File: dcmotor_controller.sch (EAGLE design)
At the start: 69 parts, among them IC1 L298, IC2 L298, IC3 AS5040, IC4 7805DT, IC5 SN74LVCR162245A, Q1 8MHz, U1 STM32F051C8T6

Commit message: Add files via upload
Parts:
- removed C15: 4u7, rcl:C-EU025-024X044
- removed C17, C18: 100n, rcl:C-EU025-024X044
- removed C19: 1u, rcl:C-EU025-024X044
- removed C23, C24: (no value), rcl:C-EU025-024X044
- removed C6: 10uF, rcl:CPOL-EUE1.8-4
- removed C7, C8: 1uF, rcl:CPOL-EUE1.8-4
- removed IC3: AS5040, austriamicrosystems:AS5040
- removed IC4: 7805DT, linear:7805DT
- removed LED1: (no value), led:LED
- removed R1: 10k, rcl:R-EU_0204/2V
- removed R17, R18: 10k, resistor:R-EU_0204/5
- removed R2: 330, rcl:R-EU_0204/2V
- removed R9: 4.7k, rcl:R-EU_0204/2V
- removed SV1: (no value), con-ml:ML10L
- removed U1: STM32F051C8T6, untitled:STM32F051C8T6
- added C25: 4u7, rcl:C-EU025-024X044
- added C26, C27, C28, C30: 100n, rcl:C-EU025-024X044
- added C29: 1u, rcl:C-EU025-024X044
- added C31, C32: 20p, rcl:C-EU025-024X044
- added D19: SK38SMA, diode:DIODE-DO214AC
- added F2: 2920L050, polyfuse-smd_10:2920L050
- added LED, POWER_CON: (no value), con-ptr500:AK500/2
- added LED2: (no value), led:LEDCHIPLED_0805
- added Q2: 8MHz, crystal:CSM-7X-DU
- added R19: 1.2k, 0.5W, rcl:R-EU_R2010
- added R20: 0R25, rcl:R-EU_R2512
- added R45, R63: 10k, resistor:R-EU_M0805
- added R46: 2k2, resistor:R-EU_M0805
- added R48: 100k, resistor:R-EU_M0805
- added R49: 100, resistor:R-EU_M0805
- added SV2, SV3, SV4, SV5: (no value), con-ml:ML10L
- added SV6: (no value), con-lsta:FE20-2
- added T1: BC857BS, NXP_60_26022015:BC857BS
- added T14: BSS306N, we-transistor:MOSFET-N-SOT23
- added U$1: DC-DC-STEP-DOWN-LM2596, lm2596:DC-DC-STEP-DOWN-LM2596
- added U2: STM32F10XRXT6, stm32:STM32F10XRXT6
- added X3: (no value), con-phoenix-254:MPT2
- C1: device capacitor-wima:C2,5-3 -> rcl:C-EUC0805
- C10: value 10u -> 100u; device rcl:CPOL-EU140CLH-0810 -> resistor:CPOL-EU153CLV-0807; LINK (none) -> http://www.tme.eu/pl/details/sc1e107m0806bvr/kondensatory-e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
- C11, C12, C13, C14: device capacitor-wima:C2.5/2 -> resistor:C-EUC0805
- C16: device rcl:C-EU025-024X044 -> resistor:C-EUC0805
- C2: device capacitor-wima:C2.5/4 -> rcl:C-EUC0805
- C20: value 100n -> 47u; device rcl:C-EU025-024X044 -> resistor:C-EUC0805; LINK (none) -> http://www.tme.eu/pl/details/cl21a476mqynnng/kondensatory-m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
- C21, C22: value 20p -> 100n; device rcl:C-EU025-024X044 -> resistor:C-EUC0805
- C3: device capacitor-wima:C2,5-3 -> resistor:C-EUC0805
- C4: device capacitor-wima:C2.5/4 -> resistor:C-EUC0805
- C5: value 100n -> (none); device capacitor-wima:C2,5-3 -> rcl:C-EUC0805
- C9: value 100u -> 4u7; device rcl:CPOL-EU140CLH-0810 -> resistor:C-EUC0805
- D10, D11, D12, D13, D14, D15, D16, D2, D3, D4, D5, D6, D7, D8, D9: value GF1 -> SK38SMA; device diode:GF1 -> diode:DIODE-DO214AC; LINK (none) -> http://www.tme.eu/pl/details/sk38sma-dio/diody-schottky-smd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
- D17: value GF1 -> SMBJ5.0A-TR; device diode:GF1 -> diode:SUPPRESSOR-SMBJ
- Q1: value 8MHz -> MOSFET-PCHANNEL_SOT23-3; device crystal:CSM-7X-DU -> Simplex-DiscreteSemi:MOSFET-PCHANNEL_SOT23-3
- R15, R16: device resistor:R-EU_0204/5 -> resistor:R-EU_M0805
- R3, R4, R5: device rcl:R-EU_0204/5 -> rcl:R-EU_R2512; LINK (none) -> http://www.tme.eu/pl/details/cs2512-0r25-1%25-hp/rezystory-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
- R6: value 0R25 -> 10k; device rcl:R-EU_0204/5 -> resistor:R-EU_M0805
- R7, R8: value 4.7k -> 10k 1%; device rcl:R-EU_0204/2V -> resistor:R-EU_M0805
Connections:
- removed net A_LSB_U: IC3.A_LSB_U, SV1.2
- removed net B_DIR_V: IC3.B_DIR_V, SV1.3
- removed net D0: IC3.D0, SV1.7
- removed net INDEX_W: IC3.INDEX_W, SV1.4
- removed net N$1: IC3.MAGDEC, IC3.MAGINC, R1.1, R2.2
- removed net N$10: C7.+, R8.1, R9.2
- removed net N$13: C6.+, IC3.VDD3V3
- removed net N$2: LED1.A, R2.1
- removed net PROGRAM: IC3.PROG
- removed net PWM: IC3.PWN, R8.2, SV1.9
- removed net PWM_F: C8.+, R9.1, SV1.8
- removed net VCC: C1.2, C10.+, C2.1, C3.2, C4.1, C5.1, D11.C, D13.C, D15.C, D16.C, D3.C, D5.C, D7.C, D9.C, IC1.VCC, IC1.VS, IC2.VCC, IC2.VS, IC3.VDD5V, IC4.VO, R1.2, R10.2, R11.2, R12.2, R14.2, SV1.1
- removed net VDD: C15.1, C16.1, C17.1, C18.1, C19.1, C20.1, U1A.VDD, U1A.VDDA, U1B.VDD
- new net +3V3: SV6.17
- new net 24V: C10.+, C2.1, C4.1, C9.1, D19.C, D2.C, D3.C, D4.C, D5.C, D6.C, D7.C, D8.C, IC1.VS, IC2.VS, LED-2.KL, POWER_CON-2.KL, R19.1, R45.2, U$1.IN+, X3-1.1
- new net A_LSB_U1: SV2.2, U2PORTA_H.PA8
- new net A_LSB_U2: SV3.2, U2PORTA_H.PA9
- new net A_LSB_U3: SV4.2, U2PORTA_H.PA10
- new net A_LSB_U4: SV5.2, U2PORTA_H.PA11
- new net B_DIR_V1: SV2.3, U2PORTC_H.PC8
- new net B_DIR_V2: SV3.3, U2PORTC_H.PC9
- new net B_DIR_V3: SV4.3, U2PORTC_H.PC10
- new net B_DIR_V4: SV5.3, U2PORTC_H.PC11
- new net D01: SV2.7
- new net D02: SV3.7
- new net D03: SV4.7
- new net D04: SV5.7
- new net INDEX_W1: SV2.4, U2PORTB_H.PB12
- new net INDEX_W2: SV3.4, U2PORTB_H.PB13
- new net INDEX_W3: SV4.4, U2PORTB_H.PB14
- new net INDEX_W4: SV5.4, U2PORTB_H.PB15
- new net MISO: U2PORTB_L.PB4
- new net MOSI: U2PORTB_L.PB5
- new net N$16: U2AN_POWER.VBAT
- new net N$19: Q1.G, R8.2, T1-2.C
- new net N$20: R7.2, T1-1.B, T1-1.C, T1-2.B
- new net N$21: R48.2, R49.1, T14.G
- new net N$24: LED-1.KL, T14.D
- new net OSC_IN: C31.2, Q2.2, U2PORTD/OSC.PD0/OSC<=
- new net OSC_OUT: C32.2, Q2.1, U2PORTD/OSC.PD1/OSC=>
- new net PWM1: SV2.9
- new net PWM2: SV3.9
- new net PWM3: SV4.9
- new net PWM4: SV5.9
- new net PWM_F1: SV2.8
- new net PWM_F2: SV3.8
- new net PWM_F3: SV4.8
- new net PWM_F4: SV5.8
- new net SCK: U2PORTB_L.PB3
- net 3V3: now also C22.2, C25.1, C26.1, C27.1, C28.1, C29.1, C30.1, R10.2, R11.2, R12.2, R14.2, SV2.1, SV3.1, SV4.1, SV5.1, SV6.1, U2AN_POWER.VDDA, U2POWER.VDD_1, U2POWER.VDD_2, U2POWER.VDD_3, U2POWER.VDD_4; no longer C24.1
- net 5V: now also C1.2, C14.2, C16.1, C3.2, D17.C, IC1.VCC, IC2.VCC, Q1.S, SV6.2, SV6.4, T1-2.E; no longer C23.1
- net BAT_MEAS: now also C20.1, R45.1, R46.2, U2PORTA_L.PA4; no longer U1A.PA4
- net BOOTO: now also U2RESET.BOOT0; no longer U1B.BOOT0
- net CLK: now also SV2.6, SV3.6, SV4.6, SV5.6; no longer IC3.CLK, SV1.6
- net CSN: now also SV2.5, SV3.5, SV4.5, SV5.5; no longer IC3.CSN, R7.2, SV1.5
- net EN1_UC: now also U2PORTA_L.PA6; no longer U1A.PA6
- net EN2_UC: now also U2PORTA_L.PA7; no longer U1A.PA7
- net EN3_UC: now also U2PORTB_L.PB0; no longer U1A.PB0
- net EN4_UC: now also U2PORTB_L.PB1; no longer U1A.PB1
- net GND: now also C11.1, C12.1, C13.1, C14.1, C25.2, C26.2, C27.2, C28.2, C29.2, C30.2, C31.1, C32.1, C9.2, D11.A, D13.A, D15.A, D16.A, D9.A, LED2.C, POWER_CON-1.KL, R20.1, R46.1, R48.1, R63.2, R8.1, SV2.10, SV3.10, SV4.10, SV5.10, SV6.14, SV6.20, SV6.25, SV6.30, SV6.34, SV6.39, SV6.6, SV6.9, T14.S, U$1.IN-, U$1.OUT-, U2AN_POWER.VSSA, U2POWER.VSS_1, U2POWER.VSS_2, U2POWER.VSS_3, U2POWER.VSS_4, X3-2.1; no longer C11.2, C12.2, C13.2, C14.2, C15.2, C17.2, C18.2, C19.2, C23.2, C24.2, C6.-, C7.-, C8.-, C9.-, D2.A, D4.A, D6.A, D8.A, IC3.VSS, IC4.GND, LED1.C, R17.2, R18.1, SV1.10, U1A.VSS, U1A.VSSA, U1B.VSS
- net IN11_UC: now also U2PORTC_L.PC0; no longer U1B.PB8
- net IN12_UC: now also U2PORTC_L.PC1; no longer U1B.PB9
- net IN21_UC: now also U2PORTC_L.PC2; no longer U1A.PB10
- net IN22_UC: now also U2PORTC_L.PC3; no longer U1A.PB11
- net IN31_UC: now also U2PORTC_L.PC4; no longer U1B.PB12
- net IN32_UC: now also U2PORTC_L.PC5; no longer U1B.PB13
- net IN41_UC: now also U2PORTC_L.PC6; no longer U1B.PB14
- net IN42_UC: now also U2PORTC_L.PC7; no longer U1B.PB15
- net LED: now also R49.2, U2PORTA_L.PA5; no longer U1A.PA5
- net MOT11: now also D16.C, D19.A; no longer D2.C, D3.A
- net MOT12: now also D15.C, D2.A; no longer D4.C, D5.A
- net MOT21: now also D14.C, D3.A; no longer D6.C, D7.A
- net MOT22: now also D13.C, D4.A; no longer D8.C, D9.A
- net MOT31: now also D12.C, D5.A; no longer D10.C, D11.A
- net MOT32: now also D11.C, D6.A; no longer D12.C, D13.A
- net MOT41: now also D10.C, D7.A; no longer D14.C, D15.A
- net MOT42: now also D8.A, D9.C; no longer D16.A, D17.C
- net N$3: now also LED2.A, R19.2; no longer C9.+, IC4.VI
- net N$4: now also R16.1; no longer R18.2
- net N$5: now also F2.2, U$1.OUT+; no longer C21.2, Q1.2, U1A.PF0/OSC_IN
- net N$6: now also C5.1, F2.1, Q1.D, T1-1.E; no longer C22.2, Q1.1, U1A.PF1/OSC_OUT
- net N$7: now also R15.2; no longer R17.1
- net N$8: now also R6.2; no longer R16.1
- net N$9: now also R63.1; no longer R15.2
- net NRST: now also SV6.12, U2RESET.NRST; no longer U1A.NRST
- net RPI_CLK: now also SV6.23; no longer U1B.PB3
- net RPI_MISO: now also SV6.21; no longer U1B.PB4
- net RPI_MOSI: now also SV6.19; no longer U1B.PB5
- net RPI_RXD: now also SV6.10, U2PORTB_L.PB6; no longer U1B.PB6
- net RPI_TXD: now also SV6.8, U2PORTB_L.PB7; no longer U1B.PB7
- net SCL: now also SV6.5, U2PORTB_H.PB11; no longer U1B.PF6
- net SDA: now also SV6.3, U2PORTB_H.PB10; no longer U1B.PF7
- net SEN1: now also C21.2, R20.2, U2PORTA_L.PA0; no longer C11.1, R3.2, U1A.PA0
- net SEN2: now also C11.2, R3.2, U2PORTA_L.PA1; no longer C12.1, R4.2, U1A.PA1
- net SEN3: now also C12.2, R4.2, U2PORTA_L.PA2; no longer C13.1, R5.2, U1A.PA2
- net SEN4: now also C13.2, R5.2, U2PORTA_L.PA3; no longer C14.1, R6.2, U1A.PA3
- net SPI1_NSS: now also SV6.15, SV6.24, U2PORTA_H.PA15; no longer U1B.PA15
- net SWCLK: now also SV6.22, U2PORTA_H.PA14; no longer U1B.PA14
- net SWDIO: now also SV6.18, U2PORTA_H.PA13; no longer U1B.PA13
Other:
- note added: "BATTERY MEASURES"
- note added: "LED"
- note added: "POWER"
- note removed: "4 x Encode A5040"
- note removed: "MICROCONTROLER STM32F05"
- moved on the sheet: C10, C11, C12, C13, C14, C16, C20, C21, C22, C5, R10, R11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

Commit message: update - clean - parts
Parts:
- C25, C26, C27, C28, C29, C30, C31, C32: device rcl:C-EU025-024X044 -> rcl:C-EUC0805
- D17: value SMBJ5.0A-TR -> SMBJ5.0A
- R10, R11, R12, R13, R14: device rcl:R-EU_0204/5 -> rcl:R-EU_R0805
- renumbered POWER_CON to PWR

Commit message: 3dmodel added
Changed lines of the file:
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@@
 <part name="LED2" library="led" library_urn="urn:adsk.eagle:library:259" deviceset="LED" device="CHIPLED_0805" package3d_urn="urn:adsk.eagle:package:15821/2"/>
 <part name="GND15" library="supply1" library_urn="urn:adsk.eagle:library:371" deviceset="GND" device=""/>
-<part name="U$1" library="lm2596" library_urn="urn:adsk.eagle:library:2557020" deviceset="DC-DC-STEP-DOWN-LM2596" device="" package3d_urn="urn:adsk.eagle:package:2557271/1"/>
 <part name="D19" library="diode" deviceset="DIODE-" device="DO214AC" value="SK38SMA">
 <attribute name="LINK" value="http://www.tme.eu/pl/details/sk38sma-dio/diody-schottky-smd/diotec-semiconductor/sk38sma/"/>
@@
 <part name="Q1" library="Simplex-DiscreteSemi" deviceset="MOSFET-PCHANNEL" device="_SOT23-3"/>
 <part name="D17" library="diode" library_urn="urn:adsk.eagle:library:210" deviceset="SUPPRESSOR-" device="SMBJ" package3d_urn="urn:adsk.eagle:package:43442/2" value="SMBJ5.0A"/>
+<part name="U$1" library="lm2596" library_urn="urn:adsk.eagle:library:2557020" deviceset="DC-DC-STEP-DOWN-LM2596" device="" package3d_urn="urn:adsk.eagle:package:2557271/2"/>
 </parts>
 <sheets>
@@
 <instance part="LED2" gate="G$1" x="-248.92" y="142.24" rot="R90"/>
 <instance part="GND15" gate="1" x="-236.22" y="134.62"/>
-<instance part="U$1" gate="G$1" x="-254" y="175.26"/>
 <instance part="D19" gate="G$1" x="-487.68" y="83.82" smashed="yes" rot="R90">
 <attribute name="LINK" x="-487.68" y="83.82" size="0.8128" layer="96" rot="R90" display="off"/>
@@
 </instance>
 <instance part="D17" gate="G$1" x="-139.7" y="165.1"/>
+<instance part="U$1" gate="G$1" x="-254" y="175.26"/>
 </instances>
 <busses>
@@
 <wire x1="-231.14" y1="167.64" x2="-231.14" y2="170.18" width="0.1524" layer="91"/>
 <pinref part="U$1" gate="G$1" pin="OUT-"/>
-<wire x1="-231.14" y1="170.18" x2="-236.22" y2="170.18" width="0.1524" layer="91"/>
+<wire x1="-236.22" y1="170.18" x2="-231.14" y2="170.18" width="0.1524" layer="91"/>
 </segment>
 <segment>
@@
 <segment>
 <wire x1="-279.4" y1="185.42" x2="-279.4" y2="180.34" width="0.1524" layer="91"/>
+<label x="-279.4" y="185.42" size="1.778" layer="95" rot="R90" xref="yes"/>
 <pinref part="U$1" gate="G$1" pin="IN+"/>
 <wire x1="-279.4" y1="180.34" x2="-271.78" y2="180.34" width="0.1524" layer="91"/>
-<label x="-279.4" y="185.42" size="1.778" layer="95" rot="R90" xref="yes"/>
-</segment>
-</net>
-<net name="N$5" class="0">
-<segment>
-<pinref part="U$1" gate="G$1" pin="OUT+"/>
-<pinref part="F2" gate="G$1" pin="2"/>
-<wire x1="-236.22" y1="180.34" x2="-228.6" y2="180.34" width="0.1524" layer="91"/>
 </segment>
 </net>
@@
 </segment>
 </net>
+<net name="N$1" class="0">
+<segment>
+<pinref part="U$1" gate="G$1" pin="OUT+"/>
+<pinref part="F2" gate="G$1" pin="2"/>
+<wire x1="-236.22" y1="180.34" x2="-228.6" y2="180.34" width="0.1524" layer="91"/>
+</segment>
+</net>

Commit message: Add files via upload
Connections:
- removed net MISO: U2PORTB_L.PB4
- removed net MOSI: U2PORTB_L.PB5
- removed net SCK: U2PORTB_L.PB3
- net CLK: now also U2PORTB_H.PB8
- net CSN: now also U2PORTB_H.PB9
- net RPI_CLK: now also U2PORTB_L.PB3
- net RPI_MISO: now also U2PORTB_L.PB4
- net RPI_MOSI: now also U2PORTB_L.PB5
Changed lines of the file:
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@@
 <?xml version="1.0" encoding="utf-8"?>
 <!DOCTYPE eagle SYSTEM "eagle.dtd">
-<eagle version="8.6.0">
+<eagle version="8.7.1">
 <drawing>
 <settings>
@@
 <setting verticaltext="up"/>
 </settings>
-<grid distance="50" unitdist="mil" unit="mil" style="dots" multiple="1" display="yes" altdistance="5" altunitdist="mil" altunit="mil"/>
+<grid distance="50" unitdist="mil" unit="inch" style="dots" multiple="1" display="yes" altdistance="5" altunitdist="mil" altunit="mil"/>
 <layers>
 <layer number="1" name="Top" color="4" fill="1" visible="no" active="no"/>
@@
 <label x="-228.6" y="243.84" size="1.016" layer="95" rot="R90" xref="yes"/>
 </segment>
+<segment>
+<pinref part="U2" gate="PORTB_H" pin="PB8"/>
+<wire x1="-530.86" y1="243.84" x2="-528.32" y2="243.84" width="0.1524" layer="91"/>
+<label x="-528.32" y="243.84" size="1.016" layer="95" xref="yes"/>
+</segment>
 </net>
 <net name="CSN" class="0">
@@
 <wire x1="-228.6" y1="226.06" x2="-228.6" y2="223.52" width="0.1524" layer="91"/>
 <label x="-228.6" y="223.52" size="1.016" layer="95" rot="R270" xref="yes"/>
+</segment>
+<segment>
+<pinref part="U2" gate="PORTB_H" pin="PB9"/>
+<wire x1="-530.86" y1="241.3" x2="-528.32" y2="241.3" width="0.1524" layer="91"/>
+<label x="-528.32" y="241.3" size="1.016" layer="95" xref="yes"/>
 </segment>
 </net>
@@
 </segment>
 </net>
-<net name="SCK" class="0">
-<segment>
-<pinref part="U2" gate="PORTB_L" pin="PB3"/>
-<wire x1="-530.86" y1="269.24" x2="-528.32" y2="269.24" width="0.1524" layer="91"/>
-<label x="-528.32" y="269.24" size="1.016" layer="95" xref="yes"/>
-</segment>
-</net>
-<net name="MISO" class="0">
-<segment>
-<pinref part="U2" gate="PORTB_L" pin="PB4"/>
-<wire x1="-530.86" y1="266.7" x2="-528.32" y2="266.7" width="0.1524" layer="91"/>
-<label x="-528.32" y="266.7" size="1.016" layer="95" xref="yes"/>
-</segment>
-</net>
-<net name="MOSI" class="0">
-<segment>
-<pinref part="U2" gate="PORTB_L" pin="PB5"/>
-<wire x1="-530.86" y1="264.16" x2="-528.32" y2="264.16" width="0.1524" layer="91"/>
-<label x="-528.32" y="264.16" size="1.016" layer="95" xref="yes"/>
-</segment>
-</net>
 <net name="N$21" class="0">
 <segment>
@@
 <label x="-167.64" y="259.08" size="0.8128" layer="95" rot="R180" xref="yes"/>
 </segment>
+<segment>
+<pinref part="U2" gate="PORTB_L" pin="PB3"/>
+<wire x1="-530.86" y1="269.24" x2="-528.32" y2="269.24" width="0.1524" layer="91"/>
+<label x="-528.32" y="269.24" size="1.016" layer="95" xref="yes"/>
+</segment>
 </net>
 <net name="RPI_MISO" class="0">
@@
 <label x="-167.64" y="256.54" size="0.8128" layer="95" rot="R180" xref="yes"/>
 </segment>
+<segment>
+<pinref part="U2" gate="PORTB_L" pin="PB4"/>
+<wire x1="-530.86" y1="266.7" x2="-528.32" y2="266.7" width="0.1524" layer="91"/>
+<label x="-528.32" y="266.7" size="1.016" layer="95" xref="yes"/>
+</segment>
 </net>
 <net name="RPI_MOSI" class="0">
@@
 <label x="-167.64" y="254" size="0.8128" layer="95" rot="R180" xref="yes"/>
 </segment>
-</net>
+<segment>
+<pinref part="U2" gate="PORTB_L" pin="PB5"/>
+<wire x1="-530.86" y1="264.16" x2="-528.32" y2="264.16" width="0.1524" layer="91"/>
+<label x="-528.32" y="264.16" size="1.016" layer="95" xref="yes"/>
+</segment>
+</net>

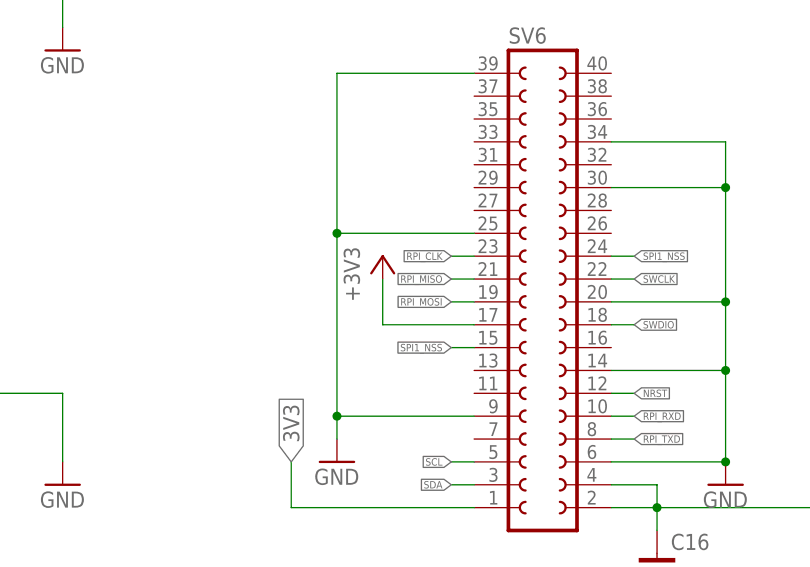
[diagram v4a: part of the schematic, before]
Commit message: some drc rules, airwires repaired and schemat checked
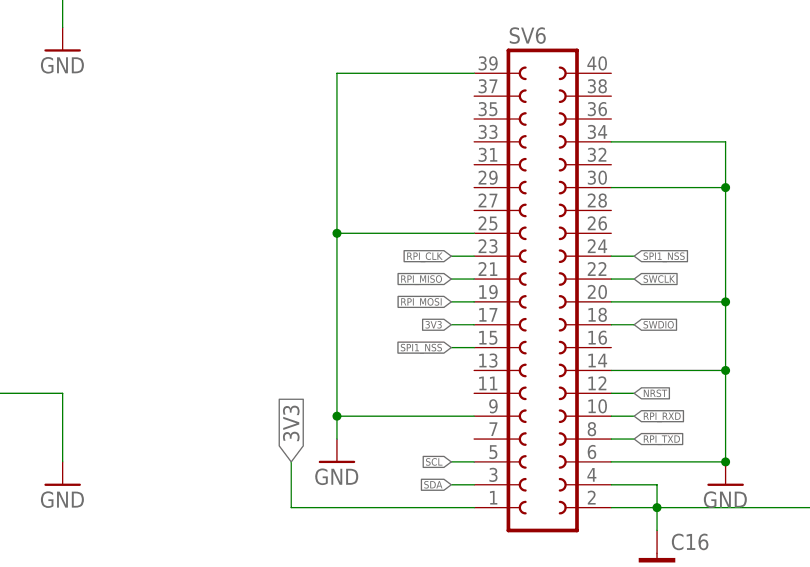
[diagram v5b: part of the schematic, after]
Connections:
- removed net +3V3: SV6.17
- net 3V3: now also SV6.17
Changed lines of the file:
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@@
 <?xml version="1.0" encoding="utf-8"?>
 <!DOCTYPE eagle SYSTEM "eagle.dtd">
-<eagle version="8.7.1">
+<eagle version="9.0.0">
 <drawing>
 <settings>
@@
 <part name="GND57" library="supply1" deviceset="GND" device=""/>
 <part name="GND58" library="supply1" deviceset="GND" device=""/>
-<part name="+3V1" library="supply1" deviceset="+3V3" device=""/>
 <part name="C16" library="resistor" library_urn="urn:adsk.eagle:library:348" deviceset="C-EU" device="C0805" package3d_urn="urn:adsk.eagle:package:26137/1" value="100n"/>
 <part name="GND59" library="supply1" deviceset="GND" device=""/>
@@
 <instance part="GND57" gate="1" x="-180.34" y="236.22"/>
 <instance part="GND58" gate="1" x="-137.16" y="233.68"/>
-<instance part="+3V1" gate="G$1" x="-175.26" y="259.08"/>
 <instance part="C16" gate="G$1" x="-144.78" y="226.06"/>
 <instance part="GND59" gate="1" x="-144.78" y="218.44"/>
@@
 <label x="-429.26" y="246.38" size="1.016" layer="95" xref="yes"/>
 </segment>
+<segment>
+<pinref part="SV6" gate="G$1" pin="17"/>
+<wire x1="-165.1" y1="251.46" x2="-167.64" y2="251.46" width="0.1524" layer="91"/>
+<label x="-167.64" y="251.46" size="0.8128" layer="95" rot="R180" xref="yes"/>
+</segment>
 </net>
 <net name="PWM_SIGNAL1" class="0">
@@
 </segment>
 </net>
-<net name="+3V3" class="0">
-<segment>
-<pinref part="SV6" gate="G$1" pin="17"/>
-<pinref part="+3V1" gate="G$1" pin="+3V3"/>
-<wire x1="-165.1" y1="251.46" x2="-175.26" y2="251.46" width="0.1524" layer="91"/>
-<wire x1="-175.26" y1="251.46" x2="-175.26" y2="256.54" width="0.1524" layer="91"/>
-</segment>
-</net>

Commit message: Add files via upload
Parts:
- removed C22: 100n, resistor:C-EUC0805
- removed IC5: SN74LVCR162245A, texas:SN74LVCR162245A
- removed R15, R16, R6, R63: 10k, resistor:R-EU_M0805
- added C6, C7, C8: 100n, resistor:C-EUC0805
- added R1, R62: 10k, resistor:R-EU_M0805
- added U1, U3: SN74LVC4245APWR, Texas Instruments_By_element14_Batch_1:SN74LVC4245APWR
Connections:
- removed net N$7: IC5.2!OE, R15.2
- removed net N$8: IC5.1!OE, R6.2
- removed net N$9: IC5.1DIR, R63.1
- new net N$5: R1.1, U3.DIR, U3.~OE
- net 3V3: now also C14.1, C7.1, U1.VCCB_(3.3_V), U1.VCCB_(3.3_V)_2, U3.VCCB_(3.3_V), U3.VCCB_(3.3_V)_2; no longer C22.2, IC5.VCC, IC5.VCC@1
- net 5V: now also C6.1, C8.1, U1.(5_V)_VCCA, U3.(5_V)_VCCA; no longer C14.2, IC5.VCC@2, IC5.VCC@3
- net EN1_UC: now also U1.B1; no longer IC5.1B7
- net EN2_UC: now also U1.B2; no longer IC5.1B8
- net EN3_UC: now also U1.B3; no longer IC5.2B1
- net EN4_UC: now also U1.B4; no longer IC5.2B2
- net GND: now also C14.2, C6.2, C7.2, C8.2, R1.2, R62.2, U1.GND, U1.GND_2, U1.GND_3, U3.GND, U3.GND_2, U3.GND_3; no longer C14.1, C22.1, IC5.GND, IC5.GND@1, IC5.GND@2, IC5.GND@3, IC5.GND@4, IC5.GND@5, IC5.GND@6, IC5.GND@7, R15.1, R16.2, R6.1, R63.2
- net IN11: now also U3.A1; no longer IC5.1A3
- net IN11_UC: now also U3.B1; no longer IC5.1B3
- net IN12: now also U3.A2; no longer IC5.1A4
- net IN12_UC: now also U3.B2; no longer IC5.1B4
- net IN21: now also U3.A3; no longer IC5.1A5
- net IN21_UC: now also U3.B3; no longer IC5.1B5
- net IN22: now also U3.A4; no longer IC5.1A6
- net IN22_UC: now also U3.B4; no longer IC5.1B6
- net IN31: now also U1.A5; no longer IC5.2A3
- net IN31_UC: now also U1.B5; no longer IC5.2B3
- net IN32: now also U1.A6; no longer IC5.2A4
- net IN32_UC: now also U1.B6; no longer IC5.2B4
- net IN41: now also U1.A7; no longer IC5.2A5
- net IN41_UC: now also U1.B7; no longer IC5.2B5
- net IN42: now also U1.A8; no longer IC5.2A6
- net IN42_UC: now also U1.B8; no longer IC5.2B6
- net N$4: now also R62.1, U1.DIR, U1.~OE; no longer IC5.2DIR, R16.1
- net PWM_SIGNAL1: now also U1.A1; no longer IC5.1A7
- net PWM_SIGNAL2: now also U1.A2; no longer IC5.1A8
- net PWM_SIGNAL3: now also U1.A3; no longer IC5.2A1
- net PWM_SIGNAL4: now also U1.A4; no longer IC5.2A2
- net SCL: now also U2PORTB_H.PB10; no longer U2PORTB_H.PB11
- net SDA: now also U2PORTB_H.PB11; no longer U2PORTB_H.PB10
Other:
- note added: "B to A"
- moved on the sheet: C1, C11, C12, C13, C14, C2, C21, C3, C4, D10, D11, D12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

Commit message: Add files via upload
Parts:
- added C15, C17: 100n, resistor:C-EUC0805
- added C18, C19: 10u, resistor:CPOL-EU153CLV-0807
- added U4: MCP1825S-3302E/DB, MCP1825S-3302E_DB:MCP1825S-3302E/DB
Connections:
- net 3V3: now also C17.1, C19.+, U4.VOUT; no longer SV6.1, SV6.17
- net 5V: now also C15.1, C18.+, U4.VIN
- net D01: now also U2PORTC_H.PC12
- net D02: now also U2PORTC_H.PC13
- net D03: now also U2PORTC_H.PC14
- net D04: now also U2PORTC_H.PC15
- net GND: now also C15.2, C17.2, C18.-, C19.-, U4.GND_(TAB), U4.GND_(TAB)_2
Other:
- moved on the sheet: LED2, R19
